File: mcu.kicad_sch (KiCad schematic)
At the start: 29 parts, among them J1 I2C EKRAN, Q1 BC817, SW1 SW_Push, SW2 SW_Push, U1 STM32F205VGTx, Y1 8MHz

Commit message: MCU PAGE FINISHED
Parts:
- added C31, C32: 2.2µF, symbol Device:C
- added R13: 4.7K, symbol Device:R
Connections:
- net GND: now also C31.2, C32.2
- net BT_TX: now reaches U1.47 (PB10)
- net BT_RX: now reaches U1.48 (PB11)
- net at U1.49 (VCAP_1): now also C31.1
- net HALL_A: now reaches U1.63 (PC6)
- net HALL_B: now reaches U1.64 (PC7)
- net HALL_C: now reaches U1.65 (PC8)
- net at U1.67 (PA8): now also R13.1
- net USB_ID: now reaches U1.68 (PA9)
- net USB_ID: now also U1.69 (PA10)
- net USB_DM: now reaches U1.70 (PA11)
- net USB_DP: now reaches U1.71 (PA12)
- net SWDIO: now reaches U1.72 (PA13)
- net at U1.73 (VCAP_2): now also C32.1
- net SWCLK: now reaches U1.76 (PA14)
- net CAN_RX: now reaches U1.95 (PB8)
- net CAN_TX: now reaches U1.96 (PB9)
- new net USB_VBUS: R13.2
- no-connect marks 0 -> 49
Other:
- moved on the sheet: C29, C30, Y1

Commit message: SCHEMATIC DONE - NEED REVIEW
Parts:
- removed R13: 4.7K, symbol Device:R
- BZ1: footprint (none) -> Buzzer_Beeper:Buzzer_12x9.5RM7.6
- C18, C19, C20, C21, C22, C23, C24: footprint (none) -> Capacitor_SMD:C_1210_3225Metric_Pad1.33x2.70mm_HandSolder
- C25: footprint (none) -> Capacitor_THT:C_Radial_D12.5mm_H25.0mm_P5.00mm
- C26, C28: footprint (none) -> Capacitor_THT:C_Disc_D10.5mm_W5.0mm_P5.00mm
- C27: footprint (none) -> Capacitor_THT:C_Radial_D6.3mm_H5.0mm_P2.50mm
- C29, C30: footprint (none) -> Capacitor_SMD:C_0603_1608Metric_Pad1.08x0.95mm_HandSolder
- C31, C32: footprint (none) -> Capacitor_THT:C_Rect_L7.2mm_W8.5mm_P5.00mm_FKP2_FKP2_MKS2_MKP2
- D3: footprint (none) -> LED_THT:LED_D1.8mm_W3.3mm_H2.4mm
- FB1: footprint (none) -> Resistor_SMD:R_0805_2012Metric_Pad1.20x1.40mm_HandSolder
- J1: footprint (none) -> Connector_PinSocket_2.00mm:PinSocket_1x04_P2.00mm_Vertical
- R10, R11, R12, R7, R8, R9: footprint (none) -> Resistor_THT:R_Axial_DIN0207_L6.3mm_D2.5mm_P7.62mm_Horizontal
- SW1, SW2: footprint (none) -> Button_Switch_THT:SW_PUSH_6mm_H8mm
- Y1: footprint (none) -> Crystal:Crystal_HC18-U_Vertical
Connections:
- net +5V: now also D2.2 (A); no longer BZ1.1 (+), D2.1 (K)
- net at BZ1.2 (-), Q1.3 (C): no longer D2.2 (A)
- net BT_KEY: now reaches U1.51 (PB12)
- net BT_STATE: now reaches U1.66 (PC9)
- net USB_ID: no longer names the net of U1.68 (PA9)
- net USB_ID: no longer U1.69 (PA10)
- new net: BZ1.1 (+), D2.1 (K)
- no-connect marks 49 -> 50
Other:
- moved on the sheet: D2

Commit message: LATEST UPDATES
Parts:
- C18, C19, C20, C21, C22, C23, C24: footprint Capacitor_SMD:C_1210_3225Metric_Pad1.33x2.70mm_HandSolder -> Capacitor_SMD:C_0603_1608Metric_Pad1.08x0.95mm_HandSolder
- C25: footprint Capacitor_THT:C_Radial_D12.5mm_H25.0mm_P5.00mm -> Capacitor_SMD:C_0603_1608Metric_Pad1.08x0.95mm_HandSolder
- C26: footprint Capacitor_THT:C_Disc_D10.5mm_W5.0mm_P5.00mm -> Capacitor_SMD:C_0603_1608Metric_Pad1.08x0.95mm_HandSolder
- C27: value C -> 10uf; footprint Capacitor_THT:C_Radial_D6.3mm_H5.0mm_P2.50mm -> Capacitor_SMD:C_0805_2012Metric_Pad1.18x1.45mm_HandSolder
- C31, C32: footprint Capacitor_THT:C_Rect_L7.2mm_W8.5mm_P5.00mm_FKP2_FKP2_MKS2_MKP2 -> Capacitor_SMD:C_0603_1608Metric_Pad1.08x0.95mm_HandSolder
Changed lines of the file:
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@@
 			)
 		)
-		(property "Footprint" "Capacitor_SMD:C_1210_3225Metric_Pad1.33x2.70mm_HandSolder"
+		(property "Footprint" "Capacitor_SMD:C_0603_1608Metric_Pad1.08x0.95mm_HandSolder"
 			(at 80.9752 38.1 0)
 			(effects
@@
 			)
 		)
-		(property "Footprint" "Capacitor_SMD:C_1210_3225Metric_Pad1.33x2.70mm_HandSolder"
+		(property "Footprint" "Capacitor_SMD:C_0603_1608Metric_Pad1.08x0.95mm_HandSolder"
 			(at 21.2852 38.1 0)
 			(effects
@@
 			)
 		)
-		(property "Value" "C"
+		(property "Value" "10uf"
 			(at 148.59 40.6399 0)
 			(effects
@@
 			)
 		)
-		(property "Footprint" "Capacitor_THT:C_Radial_D6.3mm_H5.0mm_P2.50mm"
+		(property "Footprint" "Capacitor_SMD:C_0805_2012Metric_Pad1.18x1.45mm_HandSolder"
 			(at 145.7452 43.18 0)
 			(effects
@@
 			)
 		)
-		(property "Footprint" "Capacitor_SMD:C_1210_3225Metric_Pad1.33x2.70mm_HandSolder"
+		(property "Footprint" "Capacitor_SMD:C_0603_1608Metric_Pad1.08x0.95mm_HandSolder"
 			(at 68.2752 38.1 0)
 			(effects
@@
 			)
 		)
-		(property "Footprint" "Capacitor_THT:C_Rect_L7.2mm_W8.5mm_P5.00mm_FKP2_FKP2_MKS2_MKP2"
+		(property "Footprint" "Capacitor_SMD:C_0603_1608Metric_Pad1.08x0.95mm_HandSolder"
 			(at 68.2752 172.72 0)
 			(effects
@@
 			)
 		)
-		(property "Footprint" "Capacitor_THT:C_Disc_D10.5mm_W5.0mm_P5.00mm"
+		(property "Footprint" "Capacitor_SMD:C_0603_1608Metric_Pad1.08x0.95mm_HandSolder"
 			(at 129.2352 44.45 0)
 			(effects
@@
 			)
 		)
-		(property "Footprint" "Capacitor_SMD:C_1210_3225Metric_Pad1.33x2.70mm_HandSolder"
+		(property "Footprint" "Capacitor_SMD:C_0603_1608Metric_Pad1.08x0.95mm_HandSolder"
 			(at 92.4052 38.1 0)
 			(effects
@@
 			)
 		)
-		(property "Footprint" "Capacitor_SMD:C_1210_3225Metric_Pad1.33x2.70mm_HandSolder"
+		(property "Footprint" "Capacitor_SMD:C_0603_1608Metric_Pad1.08x0.95mm_HandSolder"
 			(at 55.5752 38.1 0)
 			(effects
@@
 			)
 		)
-		(property "Footprint" "Capacitor_SMD:C_1210_3225Metric_Pad1.33x2.70mm_HandSolder"
+		(property "Footprint" "Capacitor_SMD:C_0603_1608Metric_Pad1.08x0.95mm_HandSolder"
 			(at 44.1452 38.1 0)
 			(effects
@@
 			)
 		)
-		(property "Footprint" "Capacitor_THT:C_Radial_D12.5mm_H25.0mm_P5.00mm"
+		(property "Footprint" "Capacitor_SMD:C_0603_1608Metric_Pad1.08x0.95mm_HandSolder"
 			(at 117.8052 44.45 0)
 			(effects
@@
 			)
 		)
-		(property "Footprint" "Capacitor_SMD:C_1210_3225Metric_Pad1.33x2.70mm_HandSolder"
+		(property "Footprint" "Capacitor_SMD:C_0603_1608Metric_Pad1.08x0.95mm_HandSolder"
 			(at 32.7152 38.1 0)
 			(effects
@@
 			)
 		)
-		(property "Footprint" "Capacitor_THT:C_Rect_L7.2mm_W8.5mm_P5.00mm_FKP2_FKP2_MKS2_MKP2"
+		(property "Footprint" "Capacitor_SMD:C_0603_1608Metric_Pad1.08x0.95mm_HandSolder"
 			(at 61.9252 172.72 0)
 			(effects

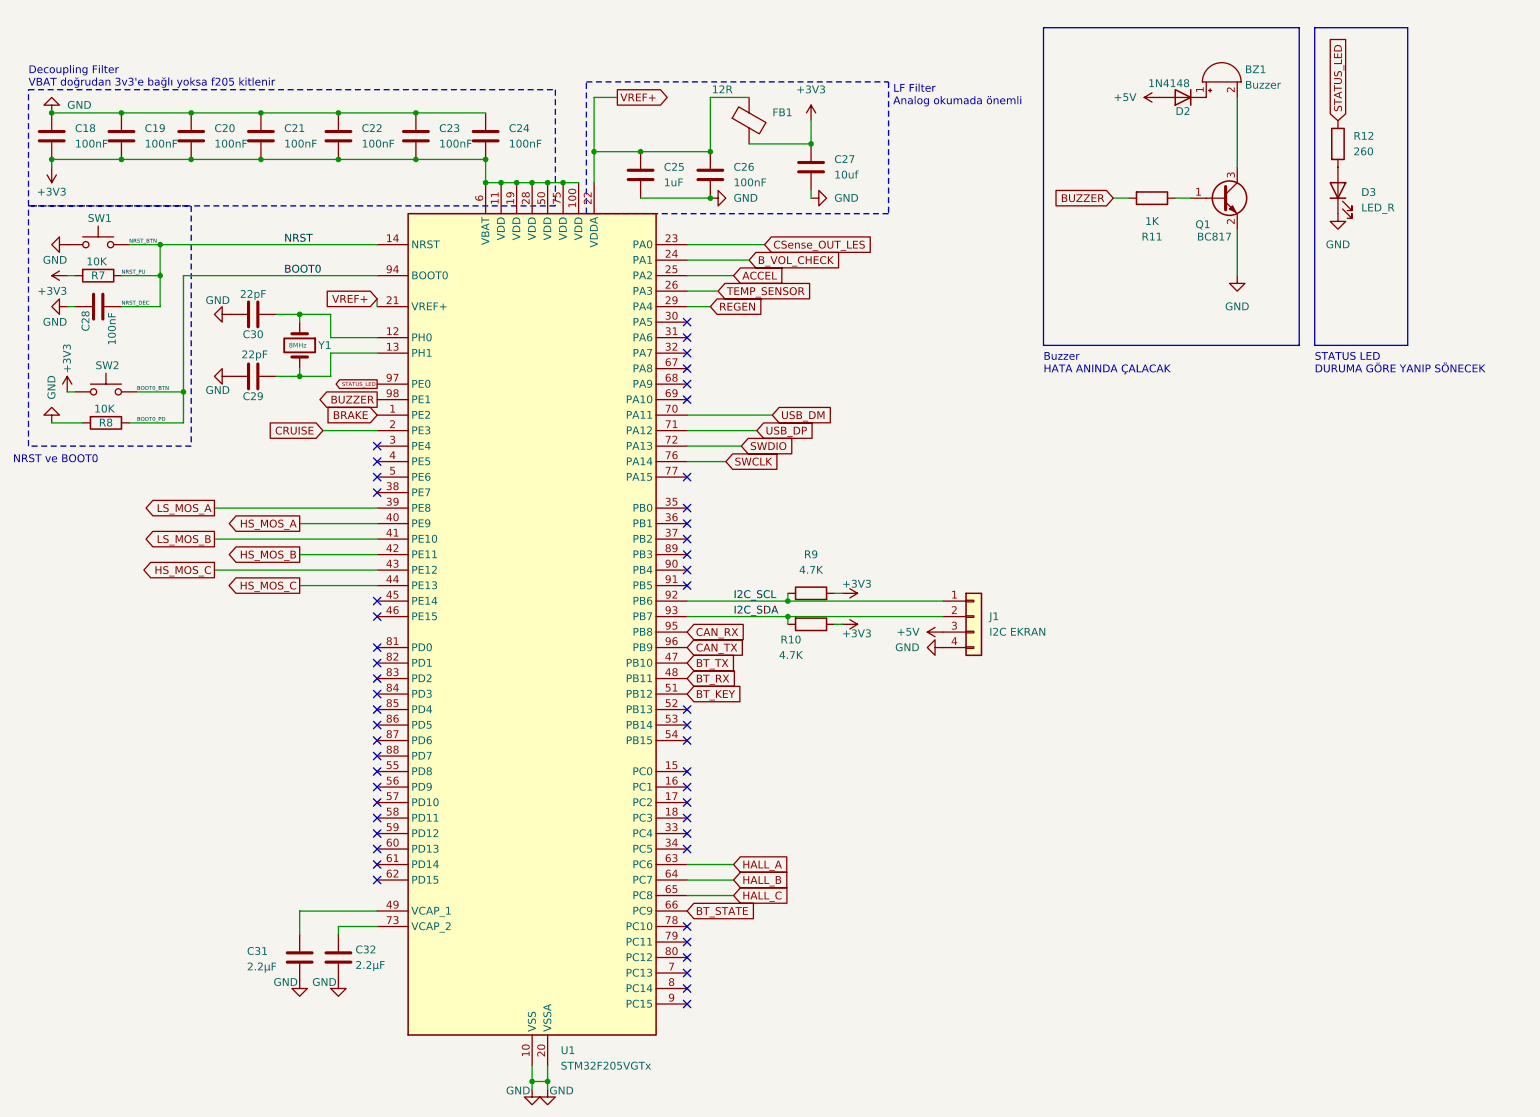
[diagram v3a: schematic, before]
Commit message: Fet Drivers  olarak IRS21867S, MOSFET olarak IAUS300N08S5N014 değiştirildi. Decoupler kısmı değiştirildi, (paraziter direnci arttırıldı.) buzzer düzeltildi ve utility kısmına alındı. CAN-BUS bitti. LDO sayısı 2x oldu
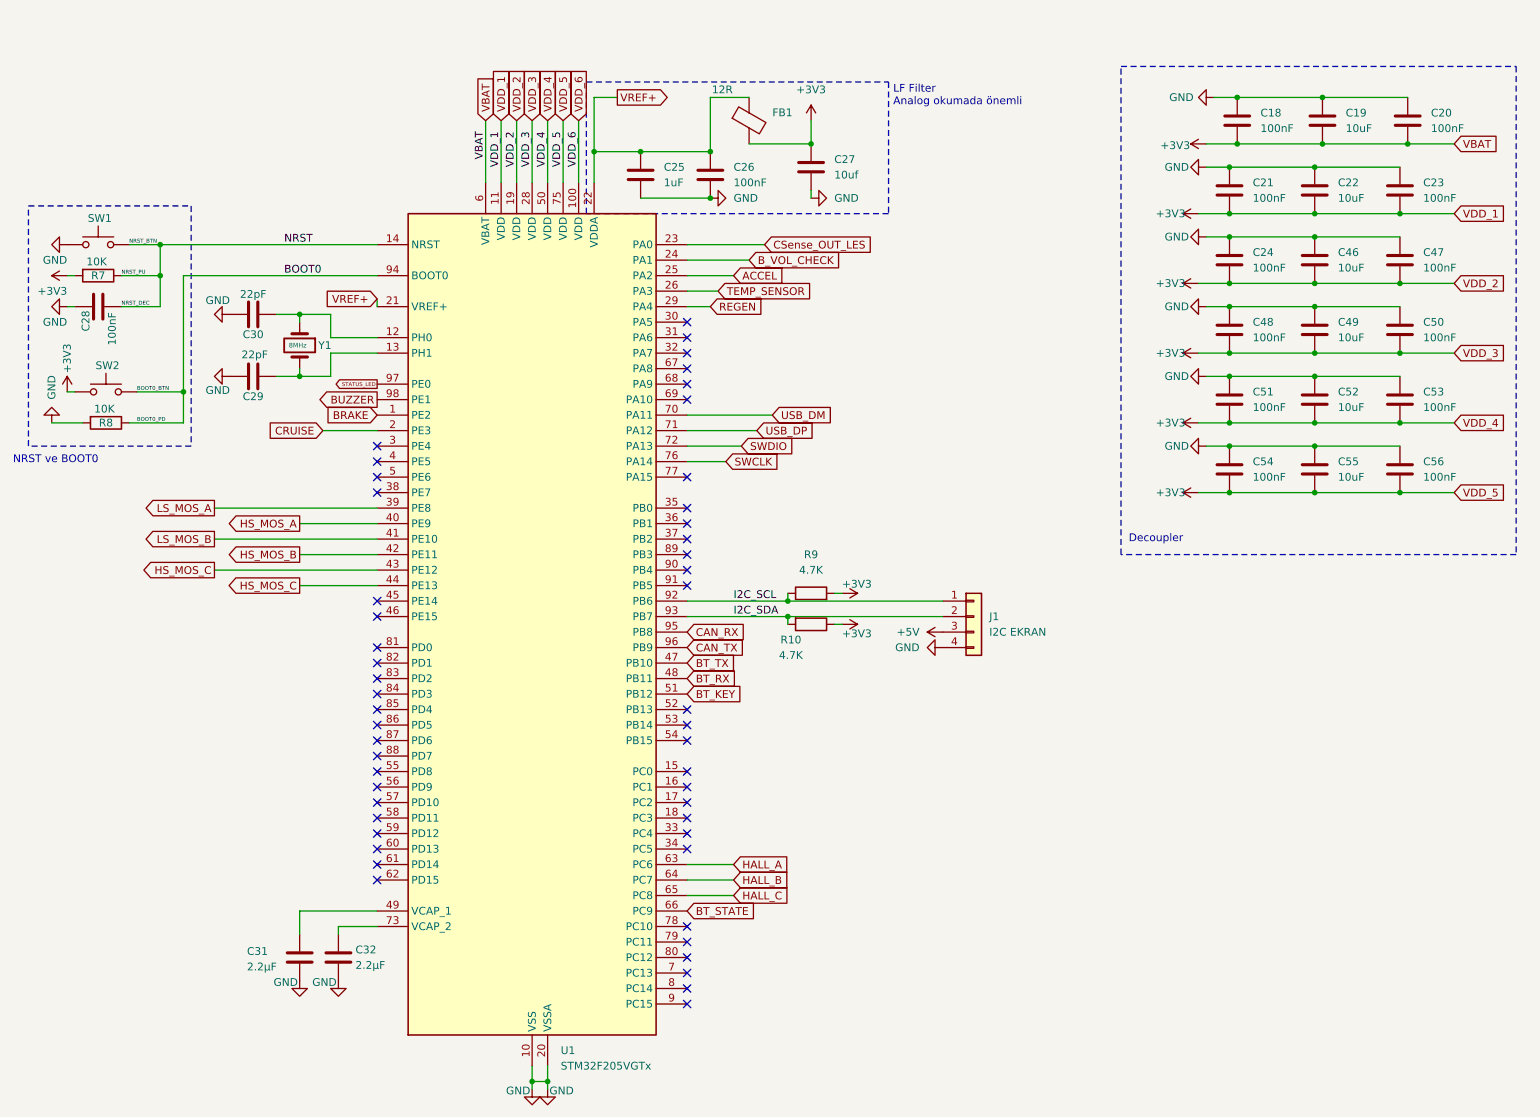
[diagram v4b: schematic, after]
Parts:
- removed BZ1: Buzzer, Buzzer_Beeper:Buzzer_12x9.5RM7.6, symbol Device:Buzzer
- removed D2: 1N4148, Diode_THT:D_DO-35_SOD27_P7.62mm_Horizontal, symbol Diode:1N4148
- removed D3: LED_R, LED_THT:LED_D1.8mm_W3.3mm_H2.4mm, symbol Device:LED
- removed Q1: BC817, Package_TO_SOT_SMD:SOT-23, symbol Transistor_BJT:BC817
- removed R11: 1K, Resistor_THT:R_Axial_DIN0207_L6.3mm_D2.5mm_P7.62mm_Horizontal, symbol Device:R
- removed R12: 260, Resistor_THT:R_Axial_DIN0207_L6.3mm_D2.5mm_P7.62mm_Horizontal, symbol Device:R
- added C46, C49, C52, C55: 10uF, Capacitor_SMD:C_0603_1608Metric_Pad1.08x0.95mm_HandSolder, symbol Device:C
- added C47, C48, C50, C51, C53, C54, C56: 100nF, Capacitor_SMD:C_0603_1608Metric_Pad1.08x0.95mm_HandSolder, symbol Device:C
- C19, C22: value 100nF -> 10uF
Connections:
- net +3V3: now also C46.2, C47.2, C48.2, C49.2, C50.2, C51.2, C52.2, C53.2, C54.2, C55.2, C56.2; no longer U1.100 (VDD)
- net GND: now also C46.1, C47.1, C48.1, C49.1, C50.1, C51.1, C52.1, C53.1, C54.1, C55.1, C56.1
- new net VDD_6: U1.100 (VDD)
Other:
- note added: "Decoupler"
- note removed: "Buzzer HATA ANINDA ÇALACAK"
- note removed: "Decoupling Filter VBAT doğrudan 3v3'e bağlı yoksa f205 kitlenir"
- note removed: "STATUS LED DURUMA GÖRE YANIP SÖNECEK"
- moved on the sheet: C18

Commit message: update Current sense
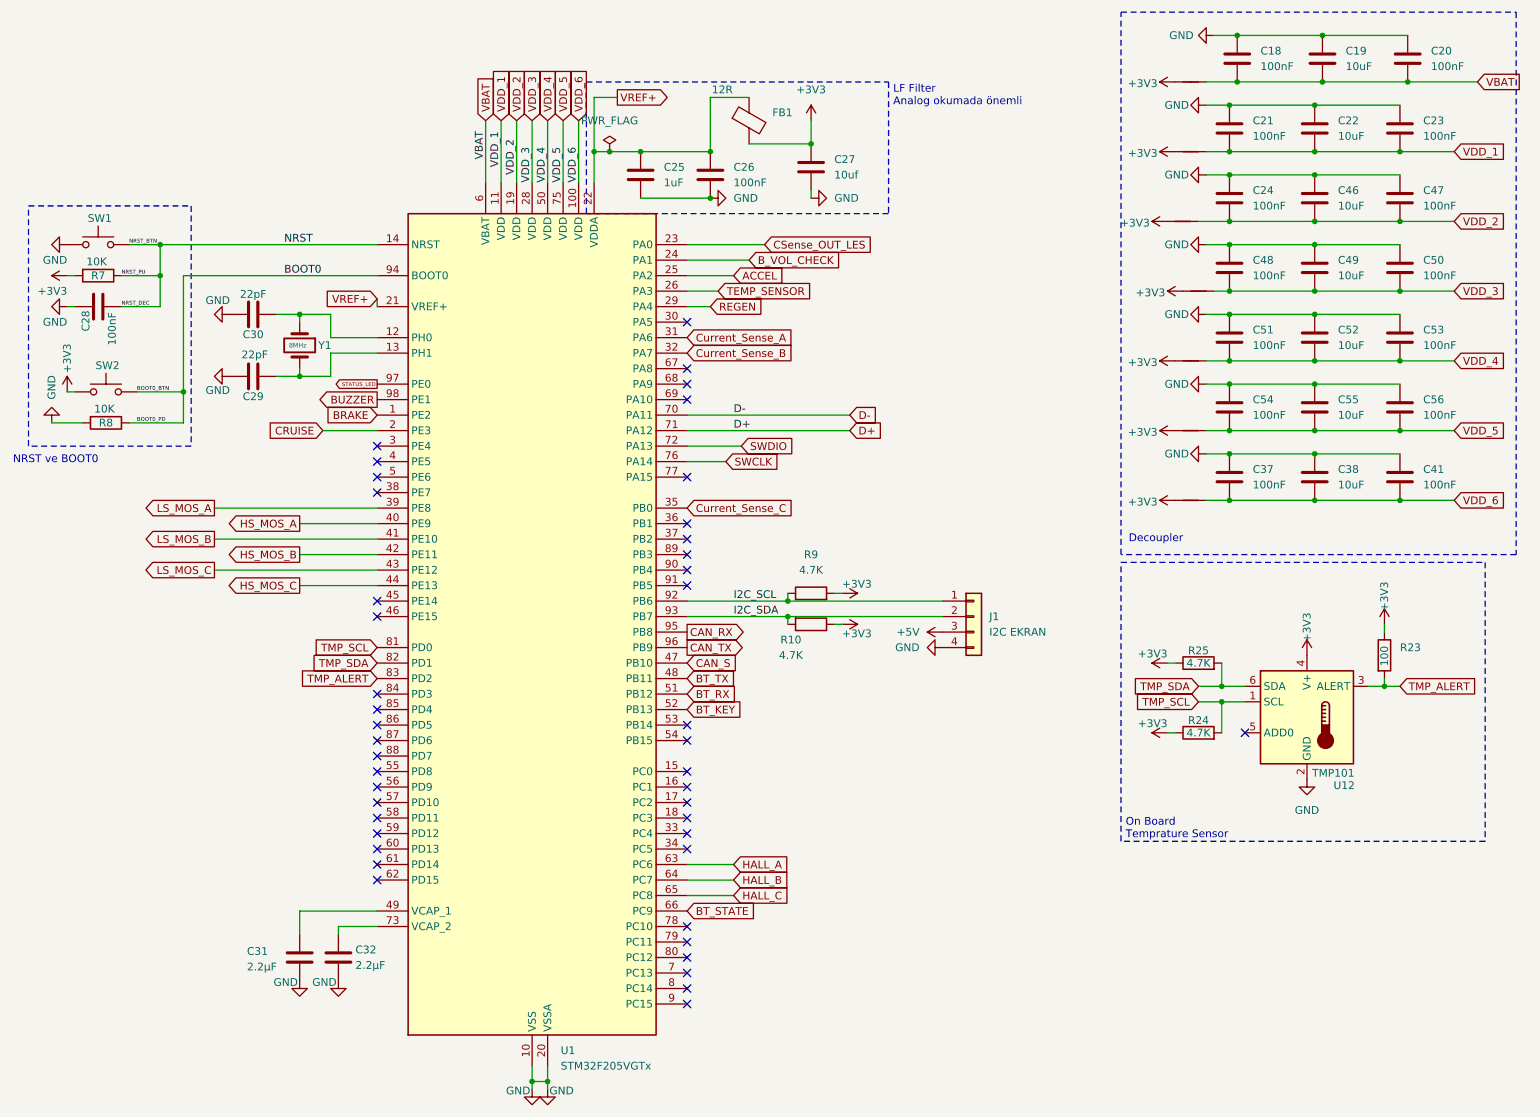
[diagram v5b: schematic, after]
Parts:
- added C37, C41: 100nF, Capacitor_SMD:C_0603_1608Metric_Pad1.08x0.95mm_HandSolder, symbol Device:C
- added C38: 10uF, Capacitor_SMD:C_0603_1608Metric_Pad1.08x0.95mm_HandSolder, symbol Device:C
- added NT2, NT3, NT4, NT5, NT6, NT7, NT9: NetTie_2, NetTie:NetTie-2_SMD_Pad0.5mm, symbol Device:NetTie_2
- added R23: 100, Resistor_SMD:R_0603_1608Metric_Pad0.98x0.95mm_HandSolder, symbol Device:R
- added R24, R25: 4.7K, Resistor_SMD:R_0603_1608Metric_Pad0.98x0.95mm_HandSolder, symbol Device:R
- added U12: TMP101, Package_TO_SOT_SMD:SOT-23-6, symbol Sensor_Temperature:TMP101
- R10, R9: footprint Resistor_THT:R_Axial_DIN0207_L6.3mm_D2.5mm_P7.62mm_Horizontal -> Resistor_SMD:R_0603_1608Metric_Pad0.98x0.95mm_HandSolder
- R8: footprint Resistor_THT:R_Axial_DIN0207_L6.3mm_D2.5mm_P7.62mm_Horizontal -> Resistor_SMD:R_0402_1005Metric_Pad0.72x0.64mm_HandSolder
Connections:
- net +3V3: now also NT2.1, NT3.1, NT4.1, NT5.1, NT6.1, NT7.1, NT9.1, R23.1, R24.1, R25.1, U12.4 (V+); no longer C18.2, C19.2, C20.2, C21.2, C22.2, C23.2, C24.2, C46.2, C47.2, C48.2, C49.2, C50.2, C51.2, C52.2, C53.2, C54.2, C55.2, C56.2, U1.11 (VDD), U1.19 (VDD), U1.28 (VDD), U1.50 (VDD), U1.6 (VBAT), U1.75 (VDD)
- net BT_KEY: now also U1.52 (PB13); no longer U1.51 (PB12)
- net BT_RX: now also U1.51 (PB12); no longer U1.48 (PB11)
- net BT_TX: now also U1.48 (PB11); no longer U1.47 (PB10)
- net GND: now also C37.1, C38.1, C41.1, U12.2 (GND)
- net HS_MOS_C: no longer U1.43 (PE12)
- net VDD_6: now also C37.2, C38.2, C41.2, NT6.2
- net Current_Sense_A: now reaches U1.31 (PA6)
- net Current_Sense_B: now reaches U1.32 (PA7)
- net Current_Sense_C: now reaches U1.35 (PB0)
- net TMP_SCL: now reaches U1.81 (PD0)
- net TMP_SCL: now also R24.2, U12.1 (SCL)
- net TMP_SDA: now reaches U1.82 (PD1)
- net TMP_SDA: now also R25.2, U12.6 (SDA)
- net TMP_ALERT: now reaches U1.83 (PD2)
- net TMP_ALERT: now also R23.2, U12.3 (ALERT)
- net USB_DM renamed D-
- net USB_DP renamed D+
- new net CAN_S: U1.47 (PB10)
- new net LS_MOS_C: U1.43 (PE12)
- new net VBAT: C18.2, C19.2, C20.2, NT2.2, U1.6 (VBAT)
- new net VDD_1: C21.2, C22.2, C23.2, NT3.2, U1.11 (VDD)
- new net VDD_2: C24.2, C46.2, C47.2, NT9.2, U1.19 (VDD)
- new net VDD_3: C48.2, C49.2, C50.2, NT5.2, U1.28 (VDD)
- new net VDD_4: C51.2, C52.2, C53.2, NT4.2, U1.50 (VDD)
- new net VDD_5: C54.2, C55.2, C56.2, NT7.2, U1.75 (VDD)
- no-connect marks 50 -> 44
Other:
- note added: "On Board Temprature Sensor"
- moved on the sheet: C18, C19, C20, C21, C22, C23, C24, C46, C47, C48, C49, C50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

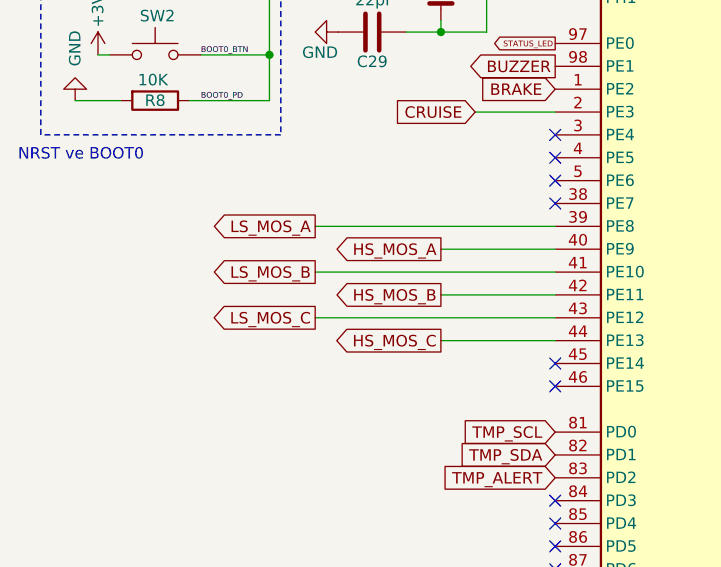
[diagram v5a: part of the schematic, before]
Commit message: update: revised label
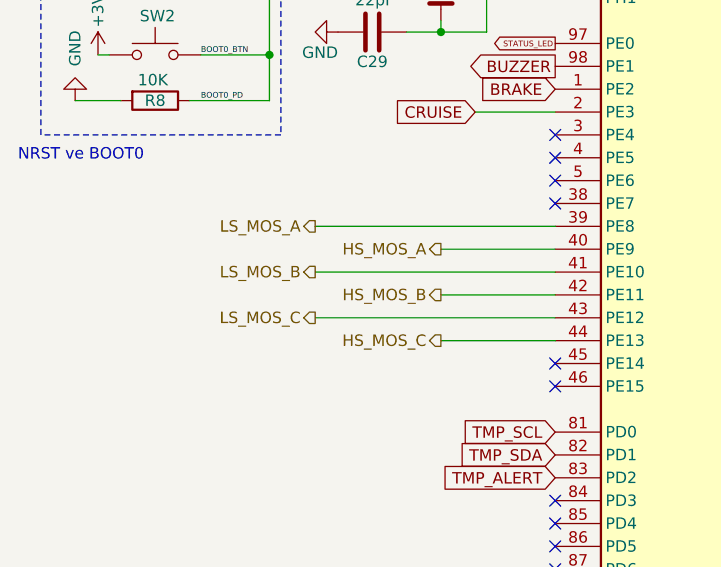
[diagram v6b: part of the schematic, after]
